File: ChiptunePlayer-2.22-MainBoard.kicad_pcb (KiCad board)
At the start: 2 copper layers, 68 parts, among them J1 Conn_01x10_Male, J2 Conn_02x10_Odd_Even, J3 USB_OTG, Q1 BC817, SW1 +, SW2 -, SW3 MENY, SW4 LEFT, SW5 UP, SW6 ENTER, SW7 DOWN, SW8 RETURN, SW9 RIGHT, U1 TP4056, U2 STMPS2151STR, U3 STM32F722ZETx, U4 W9812G6KH-6, Y1 NX3225SA-16.000M-STD-CRS-2, Y2 MC-306

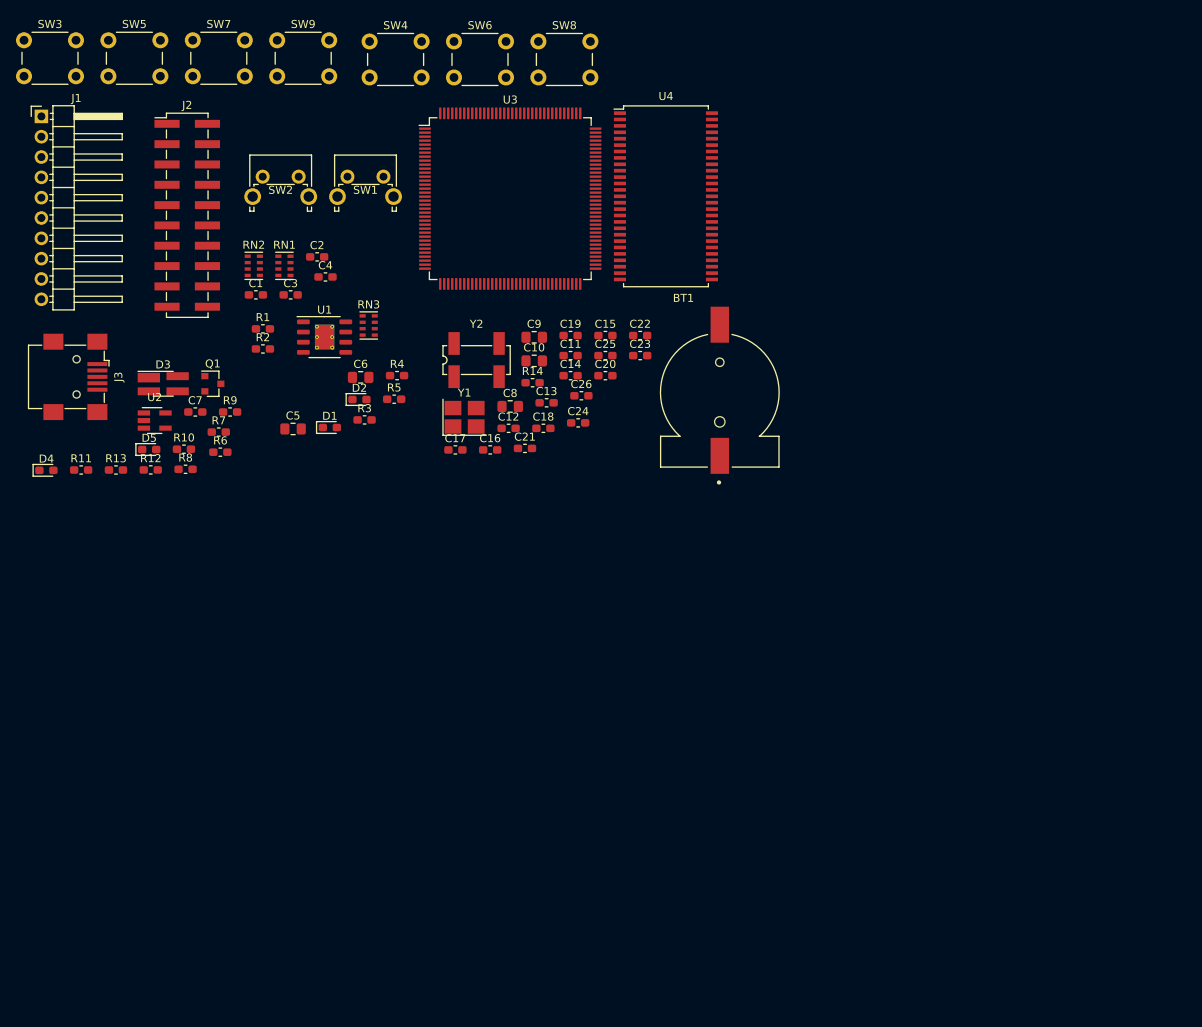
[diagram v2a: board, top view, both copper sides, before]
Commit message: Добавил LCD. Уже есть набросок формата платы с экраном и кнопками.
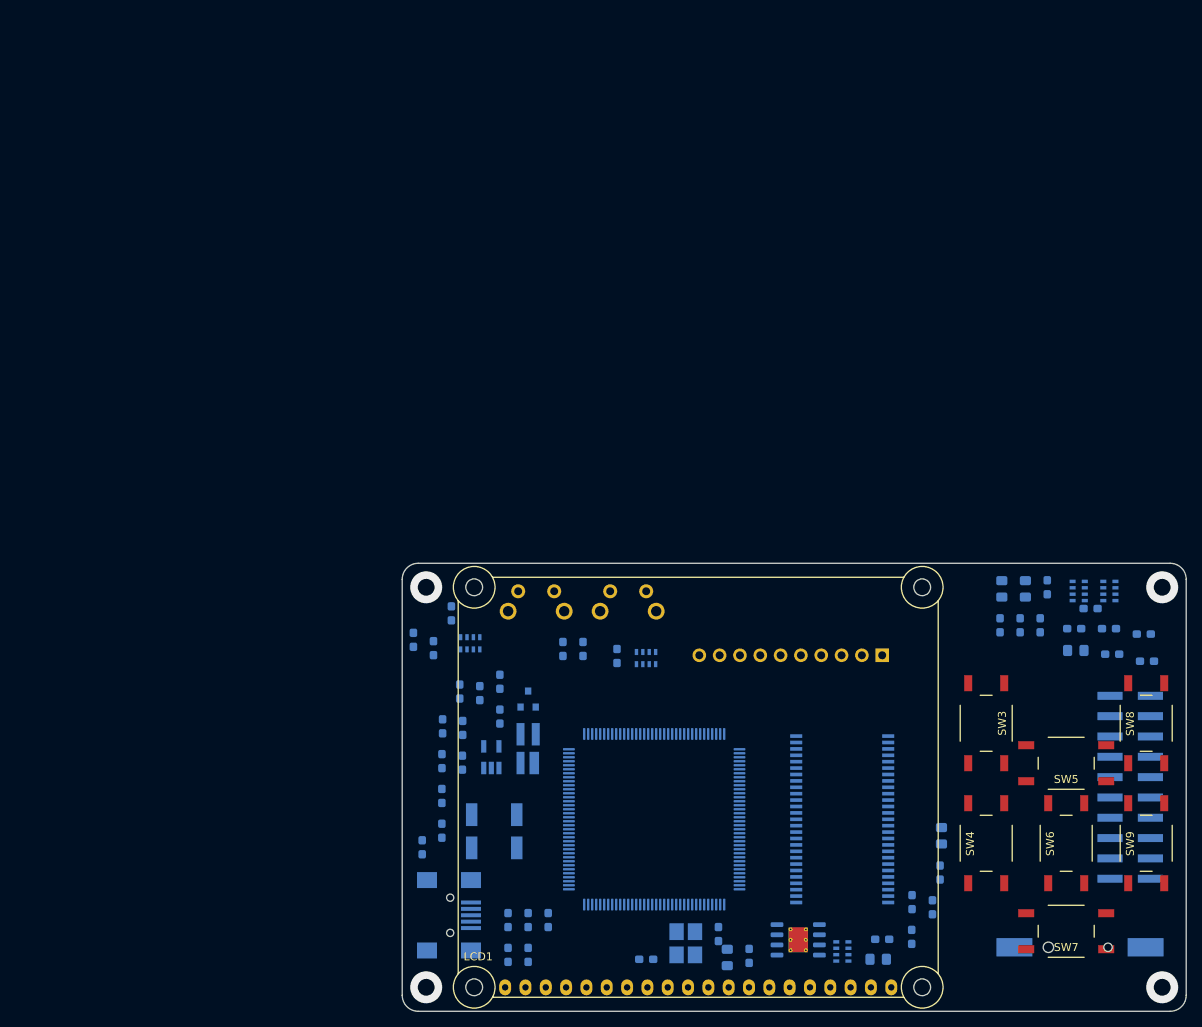
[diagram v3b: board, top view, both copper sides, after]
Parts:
- added C27: 10uF, Capacitor_SMD:C_0805_2012Metric_Pad1.15x1.40mm_HandSolder, B.Cu at (170.6, 153.3)
- added C28: 100nF, Capacitor_SMD:C_0603_1608Metric_Pad1.05x0.95mm_HandSolder, B.Cu at (173.4, 153.1)
- added LCD1: LCD_COG_12864_ST7565R_SPI, lcd:LCD_COG_12864_ST7565R, F.Cu at (137.0, 158.2)
- added RN4: CAY16-473J4, Resistor_SMD:R_Cat16-4, B.Cu at (214.6, 107.5)
- added RN5: CAY16-473J4, Resistor_SMD:R_Cat16-4, B.Cu at (218.4, 107.5)
- BT1, C1, C10, C11, C12, C13, C14, C15, C16, C17, C18, C19, C2, C20, C21, C22, C23, C24, C25, C26, C3, C4, C5, C6, C7, C8, C9, D1, D2, D3, D4, D5, J1, J2, J3, Q1, R1, R10, R11, R12, R13, R14, R2, R3, R4, R5, R6, R7, R8, R9, RN1, RN2, RN3, SW1, SW2, U1, U2, U3, U4, Y1, Y2: moved to B.Cu
- SW3, SW4, SW5, SW6, SW7, SW8, SW9: footprint Button_Switch_THT:SW_PUSH_6mm_H13mm -> button:SW_PUSH_6x6x13
- moved SW7 156.0 mm to (213.0, 150.0), turned to 180 degrees
- moved SW5 150.0 mm to (213.0, 129.0), turned to 180 degrees
- moved SW9 147.9 mm to (223.0, 139.0), turned to 90 degrees
- moved SW3 147.5 mm to (203.0, 124.0), turned to 270 degrees
- moved J2 137.9 mm to (221.0, 132.0)
- moved SW4 126.4 mm to (203.0, 139.0), turned to 90 degrees
- moved SW6 126.1 mm to (213.0, 139.0), turned to 90 degrees
- moved J1 124.8 mm to (190.0, 115.5), turned to 90 degrees
- moved SW8 114.2 mm to (223.0, 124.0), turned to 90 degrees
- moved RN3 98.1 mm to (185.0, 152.5)
- moved C6 97.3 mm to (189.5, 153.5)
- moved U1 95.8 mm to (179.5, 151.1)
- moved C5 95.7 mm to (197.4, 138.1), turned to 270 degrees
- moved D1 94.4 mm to (197.2, 142.7), turned to 270 degrees
- moved R3 93.5 mm to (196.3, 147.0), turned to 270 degrees
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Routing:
- net GND: vias 0 -> 1
- net (no net): vias 0 -> 3
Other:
- board outline added: 98 x 56 mm

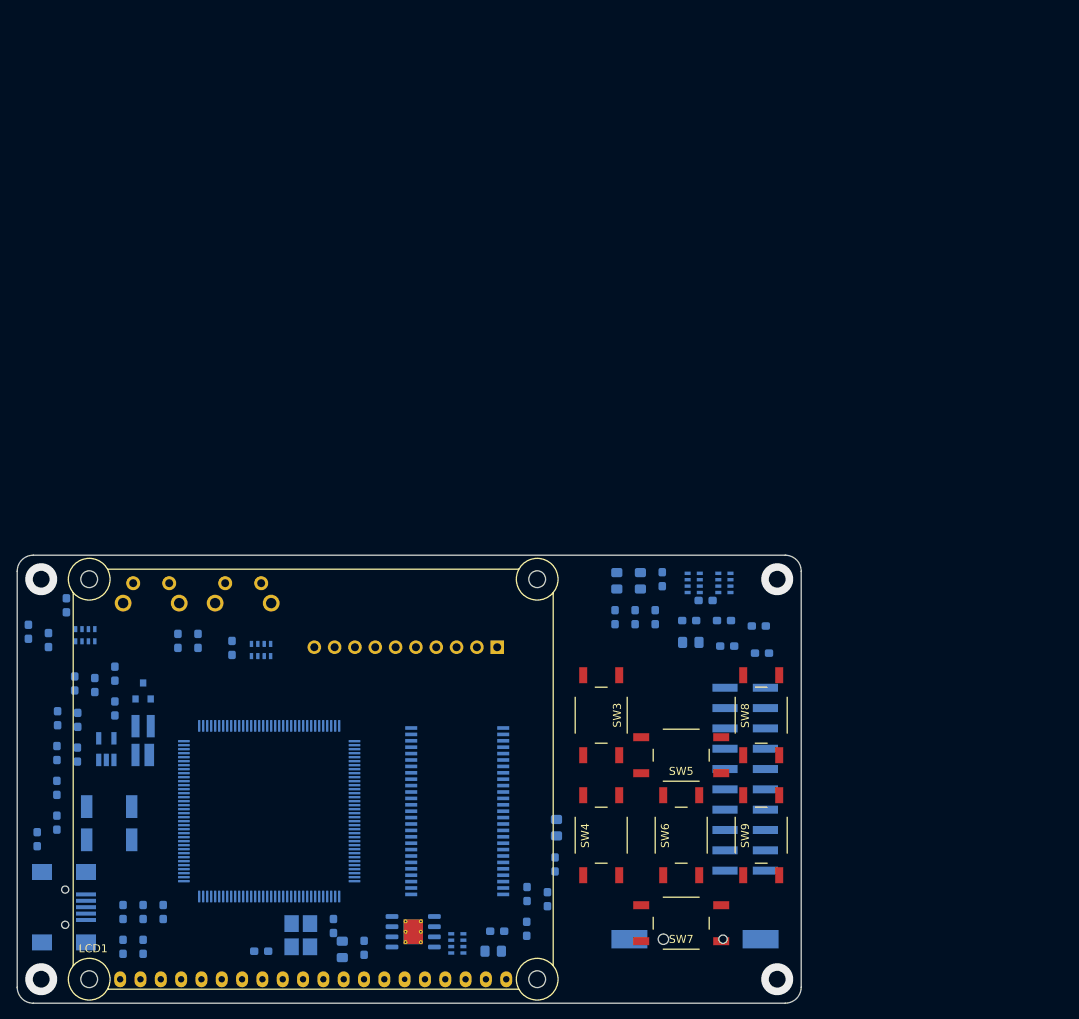
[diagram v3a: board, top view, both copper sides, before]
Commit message: dcdc доделан на 5V.
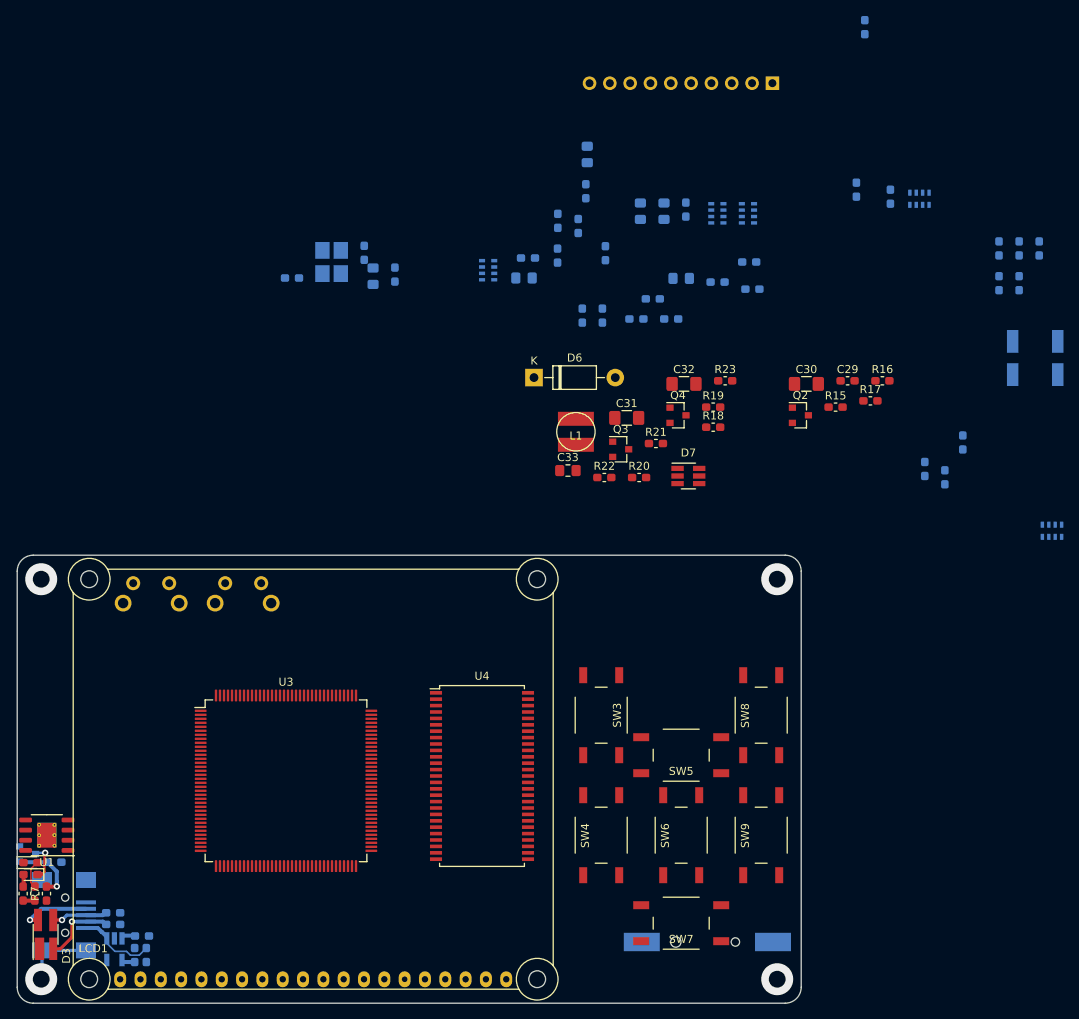
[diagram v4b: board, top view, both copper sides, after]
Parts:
- removed J2: Conn_02x10_Odd_Even, Connector_PinHeader_2.54mm:PinHeader_2x10_P2.54mm_Vertical_SMD
- added C29: 100nF, Capacitor_SMD:C_0603_1608Metric_Pad1.05x0.95mm_HandSolder, F.Cu at (233.8, 82.2)
- added C30: 2.2uF, Capacitor_SMD:C_1206_3216Metric_Pad1.42x1.75mm_HandSolder, F.Cu at (228.7, 82.6)
- added C31: 100uF, Capacitor_SMD:C_1206_3216Metric_Pad1.42x1.75mm_HandSolder, F.Cu at (206.2, 86.8)
- added C32: 10uF, Capacitor_SMD:C_1206_3216Metric_Pad1.42x1.75mm_HandSolder, F.Cu at (213.3, 82.6)
- added C33: 100nF, Capacitor_SMD:C_0805_2012Metric_Pad1.15x1.40mm_HandSolder, F.Cu at (198.8, 93.4)
- added D6: 1N5819, Diode_THT:D_DO-41_SOD81_P10.16mm_Horizontal, F.Cu at (194.6, 81.8)
- added D7: PT1301, Package_TO_SOT_SMD:SOT-23-6_Handsoldering, F.Cu at (213.9, 94.1)
- added L1: 4.7µH, inductor:CD43, F.Cu at (199.8, 88.6)
- added Q2: BC817, Package_TO_SOT_SMD:SOT-23, F.Cu at (227.9, 86.5)
- added Q3: BC817, Package_TO_SOT_SMD:SOT-23, F.Cu at (205.4, 90.8)
- added Q4: IRLML6402, Package_TO_SOT_SMD:SOT-23, F.Cu at (212.6, 86.5)
- added R15: 1K, Resistor_SMD:R_0603_1608Metric_Pad1.05x0.95mm_HandSolder, F.Cu at (232.3, 85.5)
- added R16: 10K, Resistor_SMD:R_0603_1608Metric_Pad1.05x0.95mm_HandSolder, F.Cu at (238.2, 82.2)
- added R17: 10K, Resistor_SMD:R_0603_1608Metric_Pad1.05x0.95mm_HandSolder, F.Cu at (236.7, 84.7)
- added R18: 1K, Resistor_SMD:R_0603_1608Metric_Pad1.05x0.95mm_HandSolder, F.Cu at (217.0, 88.0)
- added R19: 10K, Resistor_SMD:R_0603_1608Metric_Pad1.05x0.95mm_HandSolder, F.Cu at (217.0, 85.5)
- added R20: 4K7, Resistor_SMD:R_0603_1608Metric_Pad1.05x0.95mm_HandSolder, F.Cu at (207.7, 94.3)
- added R21: 27, Resistor_SMD:R_0603_1608Metric_Pad1.05x0.95mm_HandSolder, F.Cu at (209.8, 90.0)
- added R22: 3M, Resistor_SMD:R_0603_1608Metric_Pad1.05x0.95mm_HandSolder, F.Cu at (203.4, 94.3)
- added R23: 1M, Resistor_SMD:R_0603_1608Metric_Pad1.05x0.95mm_HandSolder, F.Cu at (218.5, 82.2)
- D3, D4, D5, R7, R8, R9, U1, U3, U4: moved to F.Cu
- moved C15 137.4 mm to (252.7, 65.7)
- moved C20 137.4 mm to (257.8, 65.7)
- moved C22 137.4 mm to (252.7, 70.0)
- moved C23 137.4 mm to (255.2, 70.0)
- moved C25 137.4 mm to (255.2, 65.7)
- moved Y2 129.5 mm to (257.2, 79.3)
- moved RN1 121.6 mm to (259.4, 101.0)
- moved R2 115.1 mm to (235.9, 38.0)
- moved C4 113.9 mm to (246.0, 94.3)
- moved C2 113.9 mm to (243.4, 93.2)
- moved C3 113.9 mm to (248.2, 89.9)
- moved C1 99.8 mm to (239.2, 59.2)
- moved R1 99.8 mm to (234.9, 58.3)
- moved RN2 99.8 mm to (242.8, 59.5)
- moved C16 84.2 mm to (164.3, 69.3)
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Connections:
- net /adc_inputs_div/ADC_CH_LEFT renamed /ADC_CH_LEFT_IN
- net /adc_inputs_div/ADC_CH_RIGHT renamed /ADC_CH_RIGHT
- net /adc_inputs_div/ADC_CH_USB_OTG_VBUS renamed /ADC_CH_OTG_VBUS
- net /adc_inputs_div/ADC_CH_VDD_BAT renamed /ADC_CH_VDD_BAT
- net /buttons/BUTTON_DOWN renamed /B_MINUS
- net /buttons/BUTTON_UP renamed /B_PLUS
- net /charging/CHRG renamed /CHRG
- net /charging/STDBY renamed /STDBY
- net /keyboard/BR1 renamed /BR1
- net /keyboard/BR2 renamed /BR2
- net /keyboard/BR3 renamed /BR3
- net /keyboard/PC3 renamed /SC3
- net /keyboard/SC1 renamed /SC1
- net /keyboard/SC2 renamed /SC2
- D3 pad 2: /usb/U_DP_+ -> /usb/U_DP_-
- D3 pad 3: /usb/U_DP_- -> /usb/U_DP_+
- LCD1 pad 5: (no net) -> /lcd/LCD_PWM
- LCD1 pad 6: (no net) -> GNDD
- LCD1 pad 7: (no net) -> VDD
- LCD1 pad 9: (no net) -> /LCD_RES
- R1 pad 2: +3V3 -> VDD
- R2 pad 2: +3V3 -> VDD
- RN1 pad 3: /ADC_LEFT_IN -> (no net)
- RN1 pad 4: /ADC_RIGHT_IN -> (no net)
- SW1 pad 1: GND -> GNDD
- SW2 pad 1: GND -> GNDD
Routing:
- net /USB_OTG_VBUS: track 0.00 -> 9.49 mm
- net /usb/U_DP_-: track 0.00 -> 9.27 mm, vias 0 -> 1
- net GND: track 0.00 -> 8.99 mm
- net /USB_ID: track 0.00 -> 8.58 mm, vias 0 -> 1
- net Net-(Q1-Pad1): track 0.00 -> 7.97 mm, vias 0 -> 1
- net /usb/U_DP_+: track 0.00 -> 7.35 mm, vias 0 -> 1
- net Net-(D5-Pad1): track 0.00 -> 4.69 mm, vias 0 -> 1
- net Net-(D4-Pad2): track 0.00 -> 3.56 mm
- net /VBUS_FAULT: track 0.00 -> 1.50 mm
- net Net-(D5-Pad2): track 0.00 -> 1.49 mm
- net /OTG_EN: track 0.00 -> 1.40 mm
- net +3V3: track 0.00 -> 1.23 mm
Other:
- rule trace_min: 0.2 -> 0.15
- rule via_min_drill: 0.3 -> 0.4
- rule via_min_size: 0.4 -> 0.6

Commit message: Сделал плату компактнее.
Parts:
- added J4: 49225-0821, microsd:49225-0821, F.Cu at (201.0, 113.2)
- added U5: YM2149, Package_DIP:DIP-40_W16.51mm_SMDSocket_LongPads, B.Cu at (195.2, 120.0)
- C27, C28, RN3, RN4, RN5: moved to F.Cu
- D3, D4, D5, R7, R8, R9: moved to B.Cu
- D6: value 1N5819 -> 1N4001; footprint Diode_THT:D_DO-41_SOD81_P10.16mm_Horizontal -> Diode_SMD:D_SMA_Handsoldering
- J1: footprint Connector_PinHeader_2.54mm:PinHeader_1x10_P2.54mm_Horizontal -> Connector_PinHeader_1.27mm:PinHeader_1x10_P1.27mm_Vertical
- moved U4 174.0 mm to (317.0, 14.7)
- moved U3 124.1 mm to (238.7, 33.4)
- moved U1 120.6 mm to (149.1, 19.4)
- moved R2 106.7 mm to (156.7, 109.4), turned to 0 degrees
- moved R1 106.3 mm to (141.7, 109.4), turned to 0 degrees
- moved R17 102.7 mm to (165.7, 159.0)
- moved C29 97.5 mm to (169.0, 155.1), turned to 180 degrees
- moved R16 95.7 mm to (180.1, 158.3), turned to 270 degrees
- moved C30 91.0 mm to (173.1, 154.7)
- moved R15 88.8 mm to (181.6, 158.3), turned to 90 degrees
- moved Q2 87.6 mm to (177.7, 158.2), turned to 180 degrees
- moved J1 83.8 mm to (142.1, 61.0)
- moved RN5 65.4 mm to (203.0, 124.0), turned to 90 degrees
- moved C27 64.2 mm to (200.6, 127.8)
- moved RN3 60.2 mm to (203.4, 126.8), turned to 270 degrees
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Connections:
- RN4 pad 7: (no net) -> /microsd/SD_CON
- RN4 pad 8: (no net) -> /microsd/SD_D1
- RN5 pad 5: (no net) -> /microsd/SD_D0
- RN5 pad 6: (no net) -> /microsd/SD_D2
- RN5 pad 7: (no net) -> /microsd/SD_D3
- RN5 pad 8: (no net) -> /microsd/SD_CMD
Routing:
- net VDD: track 0.00 -> 21.7 mm
- net /USB_OTG_VBUS: track 9.49 -> 0.00 mm
- net /usb/U_DP_-: track 9.27 -> 0.00 mm, vias 1 -> 0
- net GND: track 8.99 -> 0.00 mm
- net /USB_ID: track 8.58 -> 0.00 mm, vias 1 -> 0
- net Net-(Q1-Pad1): track 7.97 -> 0.00 mm, vias 1 -> 0
- net /usb/U_DP_+: track 7.35 -> 0.00 mm, vias 1 -> 0
- net Net-(D5-Pad1): track 4.69 -> 0.00 mm, vias 1 -> 0
- net Net-(D4-Pad2): track 3.56 -> 0.00 mm
- net /B_PLUS: track 0.00 -> 3.15 mm
- net /B_MINUS: track 0.00 -> 3.15 mm
- net Net-(Q2-Pad1): track 0.00 -> 2.90 mm
- net /microsd/SD_CON: track 0.00 -> 2.66 mm
- net /lcd/LCD_PWM: track 0.00 -> 2.22 mm
- net /microsd/SD_CMD: track 0.00 -> 2.21 mm
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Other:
- board size 98 x 56 mm -> 91 x 56 mm

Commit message: Расставил проверенные блоки в столбец.
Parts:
- added C34: 100nF, Capacitor_SMD:C_0603_1608Metric_Pad1.05x0.95mm_HandSolder, F.Cu at (181.2, 88.7)
- added C35: 100nF, Capacitor_SMD:C_0603_1608Metric_Pad1.05x0.95mm_HandSolder, F.Cu at (181.2, 91.2)
- added C36: 100nF, Capacitor_SMD:C_0603_1608Metric_Pad1.05x0.95mm_HandSolder, F.Cu at (188.9, 84.0)
- added C37: 100nF, Capacitor_SMD:C_0603_1608Metric_Pad1.05x0.95mm_HandSolder, F.Cu at (185.6, 88.7)
- added C38: 100nF, Capacitor_SMD:C_0603_1608Metric_Pad1.05x0.95mm_HandSolder, F.Cu at (185.6, 91.2)
- added C39: 100nF, Capacitor_SMD:C_0603_1608Metric_Pad1.05x0.95mm_HandSolder, F.Cu at (189.9, 86.5)
- added C40: 100nF, Capacitor_SMD:C_0603_1608Metric_Pad1.05x0.95mm_HandSolder, F.Cu at (189.9, 89.0)
- added RN6: CAT16-103J4, Resistor_SMD:R_Cat16-4, F.Cu at (177.1, 85.1)
- added RN7: CAT16-103J4, Resistor_SMD:R_Cat16-4, F.Cu at (177.1, 89.8)
- added RN8: CAT16-103J4, Resistor_SMD:R_Cat16-4, F.Cu at (180.9, 85.1)
- added RN9: CAT16-103J4, Resistor_SMD:R_Cat16-4, F.Cu at (184.8, 85.1)
- moved U4 209.6 mm to (138.6, 124.7)
- moved U3 121.7 mm to (158.6, 125.0)
- moved L1 26.5 mm to (226.3, 89.1)
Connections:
- net /ADC_CH_OTG_VBUS renamed /ADC_CH_VDD_USB
- net /VDD_BAT renamed /adc_inputs_div/VDD_BAT
- net /microsd/SD_CMD renamed /SD_CMD
- net /microsd/SD_CON renamed /SD_CON
- net /microsd/SD_D0 renamed /SD_D0
- net /microsd/SD_D1 renamed /SD_D1
- net /microsd/SD_D2 renamed /SD_D2
- net /microsd/SD_D3 renamed /SD_D3
- C5 pad 1: /USB_OTG_VBUS -> /adc_inputs_div/VDD_USB
- C7 pad 1: /USB_OTG_VBUS -> /adc_inputs_div/VDD_USB
- D1 pad 2: /USB_OTG_VBUS -> /adc_inputs_div/VDD_USB
- D2 pad 2: /USB_OTG_VBUS -> /adc_inputs_div/VDD_USB
- J3 pad 1: /USB_OTG_VBUS -> /adc_inputs_div/VDD_USB
- R6 pad 2: /USB_OTG_VBUS -> /adc_inputs_div/VDD_USB
- RN1 pad 2: /USB_OTG_VBUS -> /adc_inputs_div/VDD_USB
- U1 pad 4: /USB_OTG_VBUS -> /adc_inputs_div/VDD_USB
- U1 pad 8: /USB_OTG_VBUS -> /adc_inputs_div/VDD_USB
- U2 pad 1: /USB_OTG_VBUS -> /adc_inputs_div/VDD_USB
- U3 pad 101: /USB_OTG_VBUS -> (no net)

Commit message: Доделал цепь питания.
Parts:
- added C41: 10uF, Capacitor_SMD:C_1206_3216Metric_Pad1.42x1.75mm_HandSolder, F.Cu at (267.6, 102.3)
- added C42: 10uF, Capacitor_SMD:C_1206_3216Metric_Pad1.42x1.75mm_HandSolder, F.Cu at (267.6, 105.6)
- added C43: 100nF, Capacitor_SMD:C_0805_2012Metric_Pad1.15x1.40mm_HandSolder, F.Cu at (260.0, 106.6)
- added Q5: BC817, Package_TO_SOT_SMD:SOT-23, F.Cu at (240.5, 102.9)
- added Q6: IRLML6402, Package_TO_SOT_SMD:SOT-23, F.Cu at (240.5, 107.5)
- added R24: 1K, Resistor_SMD:R_0603_1608Metric_Pad1.05x0.95mm_HandSolder, F.Cu at (244.9, 101.9)
- added R25: 10K, Resistor_SMD:R_0603_1608Metric_Pad1.05x0.95mm_HandSolder, F.Cu at (240.4, 111.0)
- added R26: 4K7, Resistor_SMD:R_0603_1608Metric_Pad1.05x0.95mm_HandSolder, F.Cu at (249.2, 101.9)
- added R27: 27, Resistor_SMD:R_0603_1608Metric_Pad1.05x0.95mm_HandSolder, F.Cu at (244.9, 104.4)
- added SW10: PWR_ON, Button_Switch_THT:SW_Tactile_SPST_Angled_PTS645Vx83-2LFS, F.Cu at (230.7, 109.6)
- added U6: NCP551SN33T1G, Package_TO_SOT_SMD:TSOT-23-5_HandSoldering, F.Cu at (261.1, 102.9)
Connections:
- C6 pad 1: /adc_inputs_div/VDD_BAT -> /charging/VDD_BAT
- Q4 pad 2: /adc_inputs_div/VDD_BAT -> /charging/VDD_BAT
- R20 pad 1: /adc_inputs_div/VDD_BAT -> /charging/VDD_BAT
- U1 pad 5: /adc_inputs_div/VDD_BAT -> /charging/VDD_BAT
